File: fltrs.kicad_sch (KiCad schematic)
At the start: 51 parts, among them U3 CPC1117N, U4 MCP6002, U5 MCP4451-503-ST, U6 MCP6002, U7 MCP6002

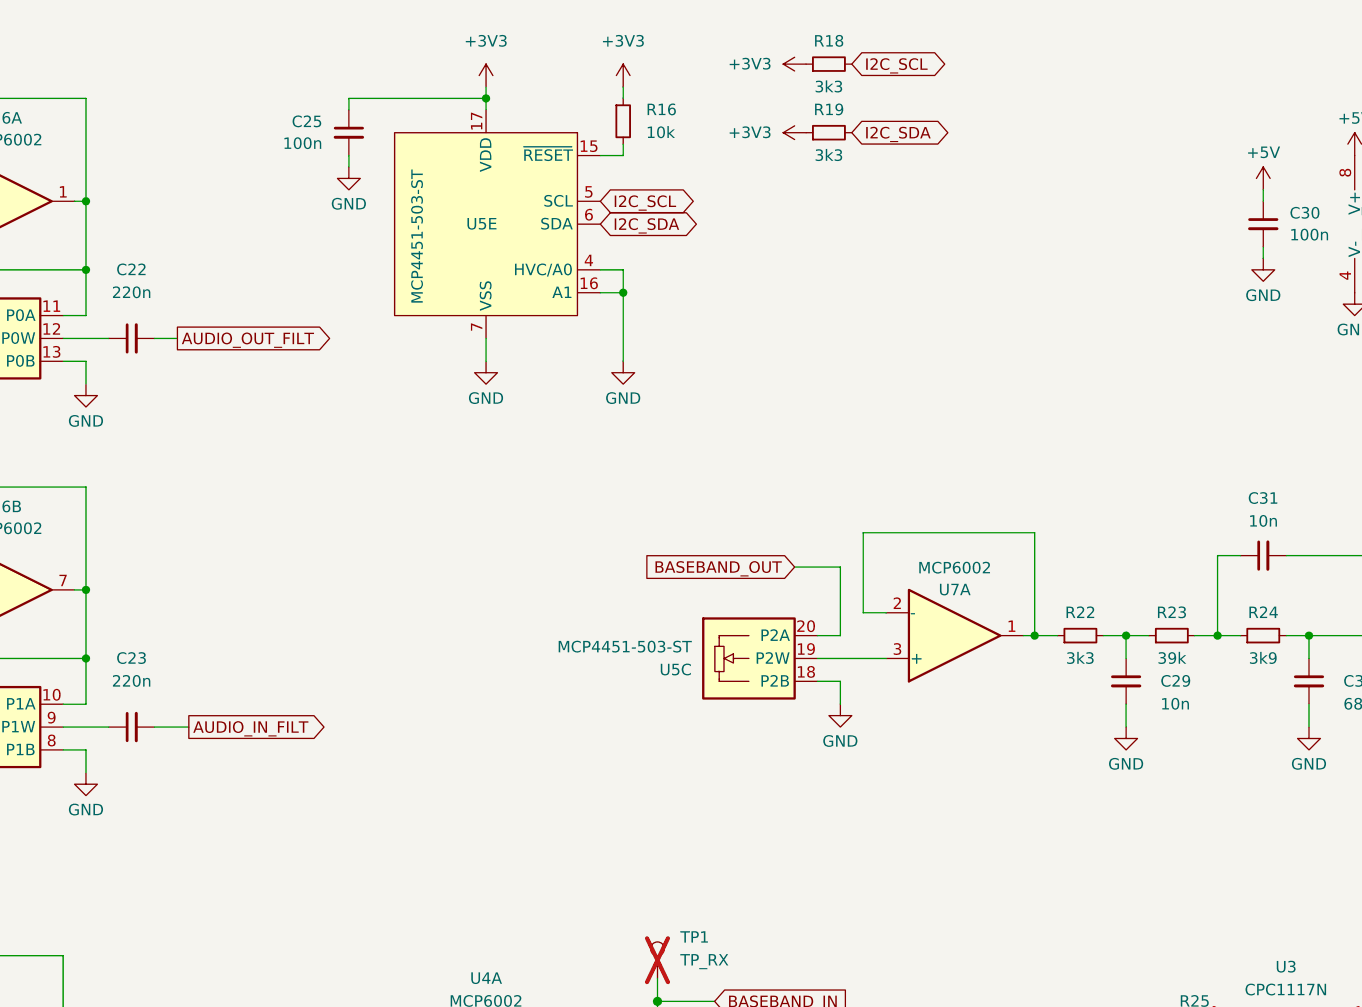
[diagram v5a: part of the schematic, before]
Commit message: PA2 Bias add, USB conn add.
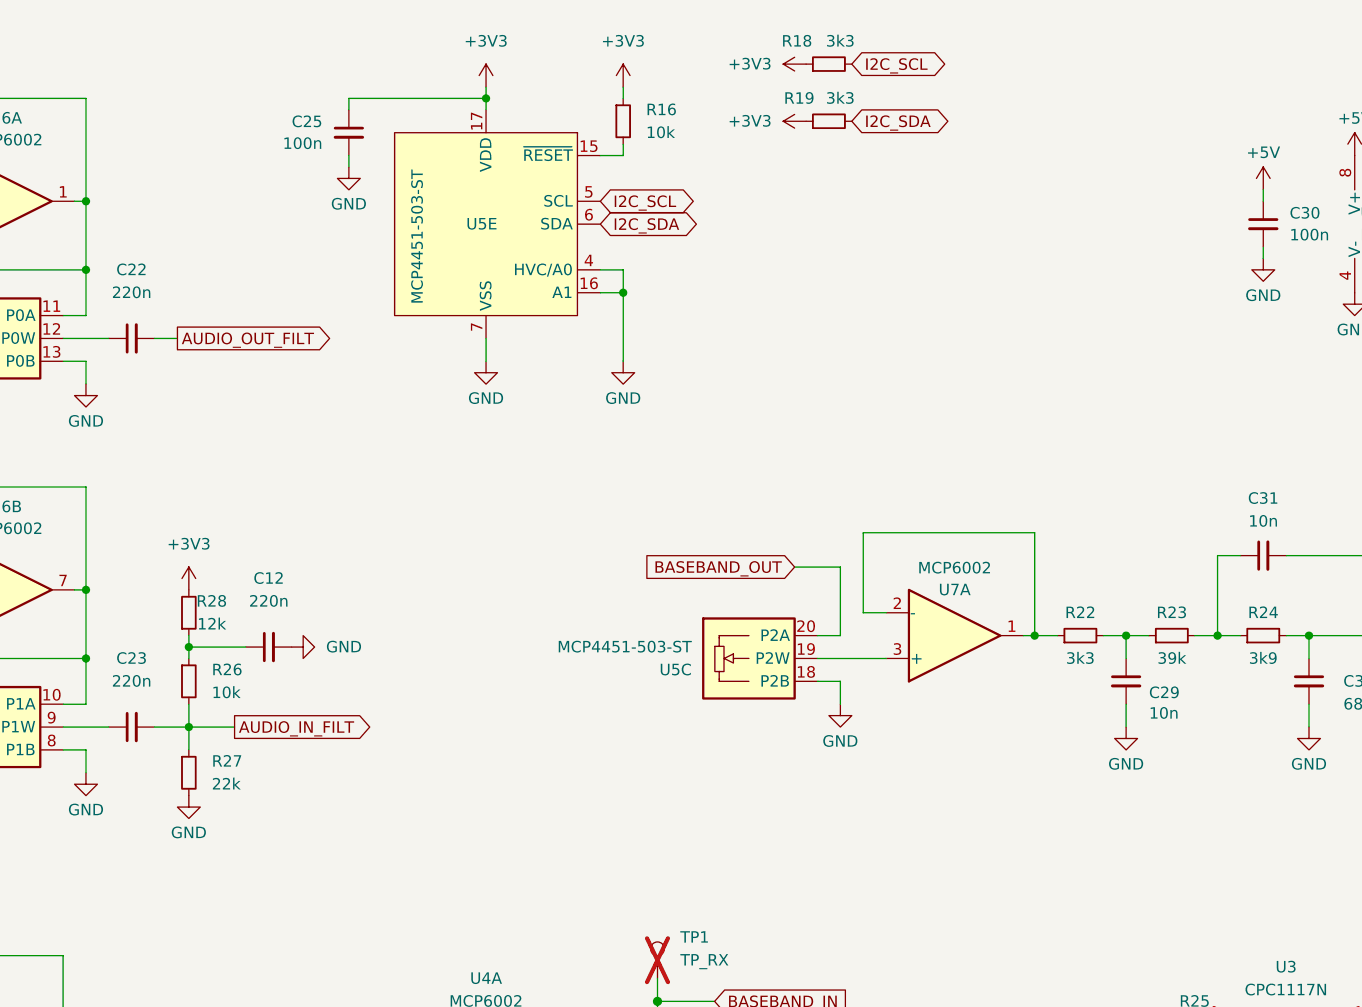
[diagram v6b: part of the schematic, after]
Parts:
- added C12: 220n, Capacitor_SMD:C_0402_1005Metric, symbol Device:C_Small
- added R26: 10k, Resistor_SMD:R_0402_1005Metric, symbol Device:R_Small
- added R27: 22k, Resistor_SMD:R_0402_1005Metric, symbol Device:R_Small
- added R28: 12k, Resistor_SMD:R_0402_1005Metric, symbol Device:R_Small
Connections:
- net +3V3: now also R28.2
- net AUDIO_IN_FILT: now also R26.2, R27.1
- net GND: now also C12.2, R27.2
- new net: C12.1, R26.1, R28.1
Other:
- title: Micro17 - OpenRTX on a Module -> Micro17 - OpenRTX on a Module for Icom Radios
- moved on the sheet: R19

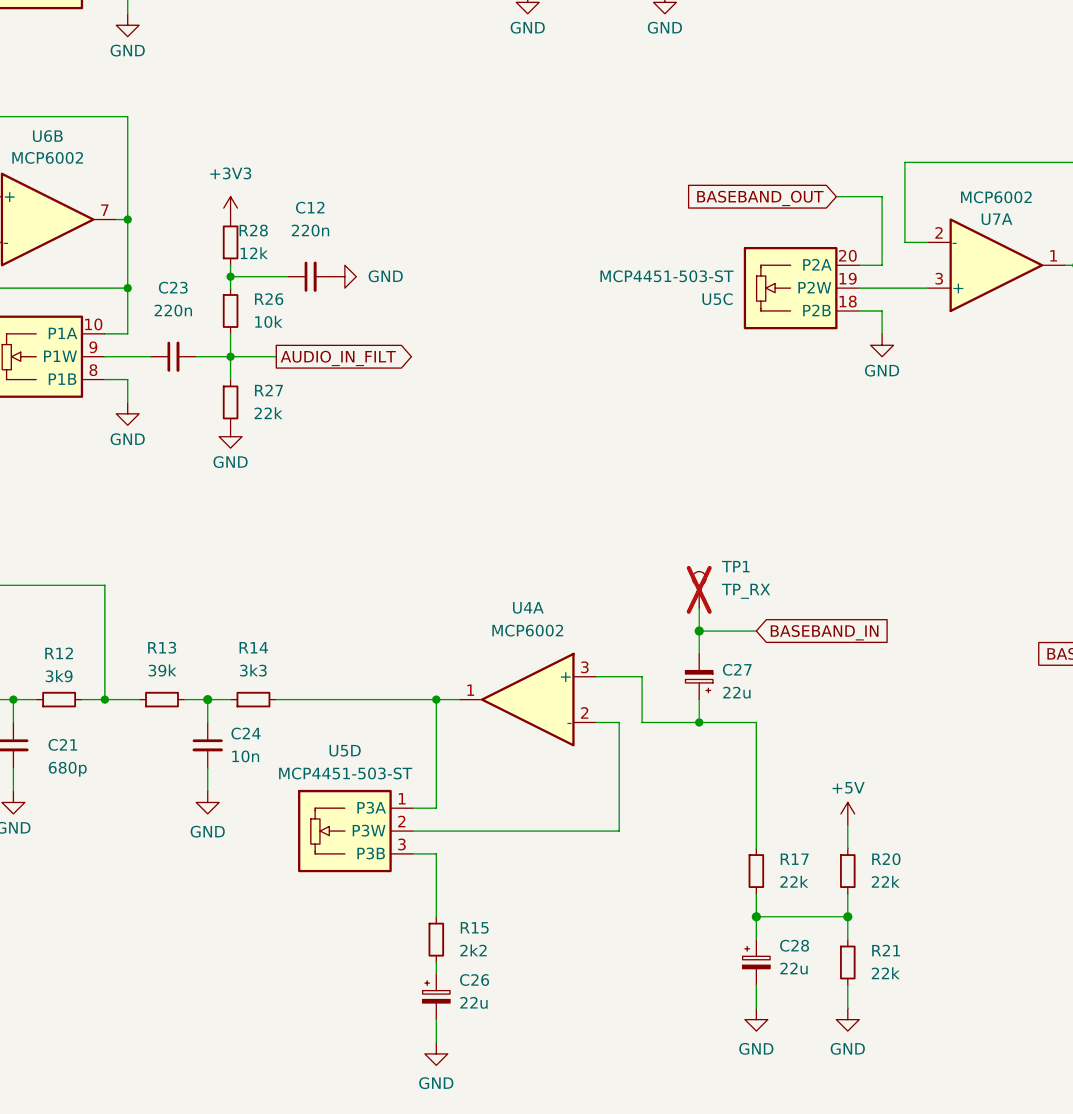
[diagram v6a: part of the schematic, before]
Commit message: Changed PA2 bias circuit
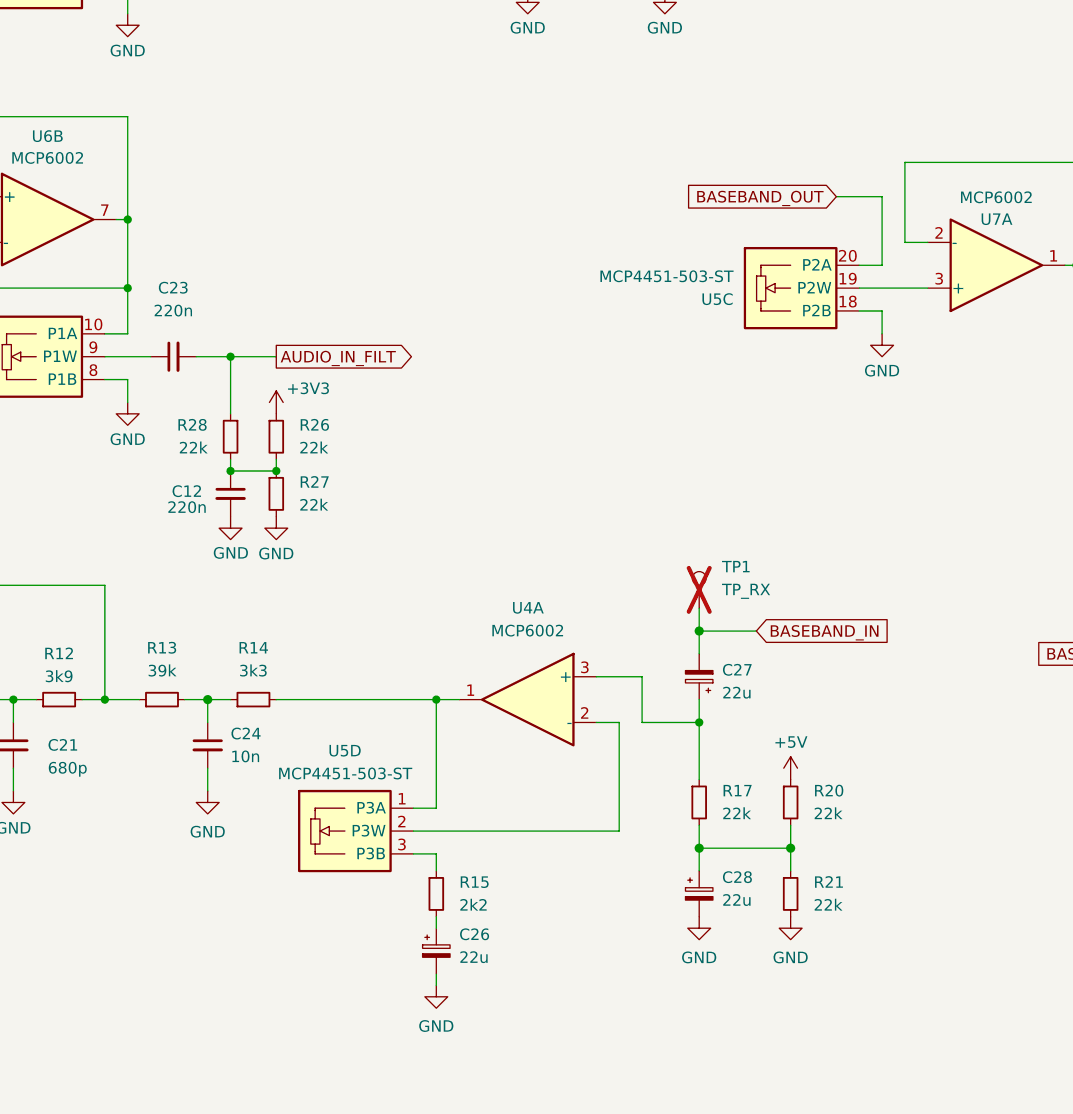
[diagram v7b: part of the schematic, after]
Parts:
- R26: value 10k -> 22k; LCSC C102749 -> C2909337; MPN (none) -> Generic R/22k/0603
- R28: value 12k -> 22k; LCSC C25752 -> C2909337; MPN (none) -> Generic R/22k/0603
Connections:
- net +3V3: now also R26.1; no longer R28.2
- net AUDIO_IN_FILT: now also R28.1; no longer R26.2, R27.1
- new net: C12.1, R26.2, R27.1, R28.2
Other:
- moved on the sheet: C12, C26, C28, R15, R17, R20, R21, R27

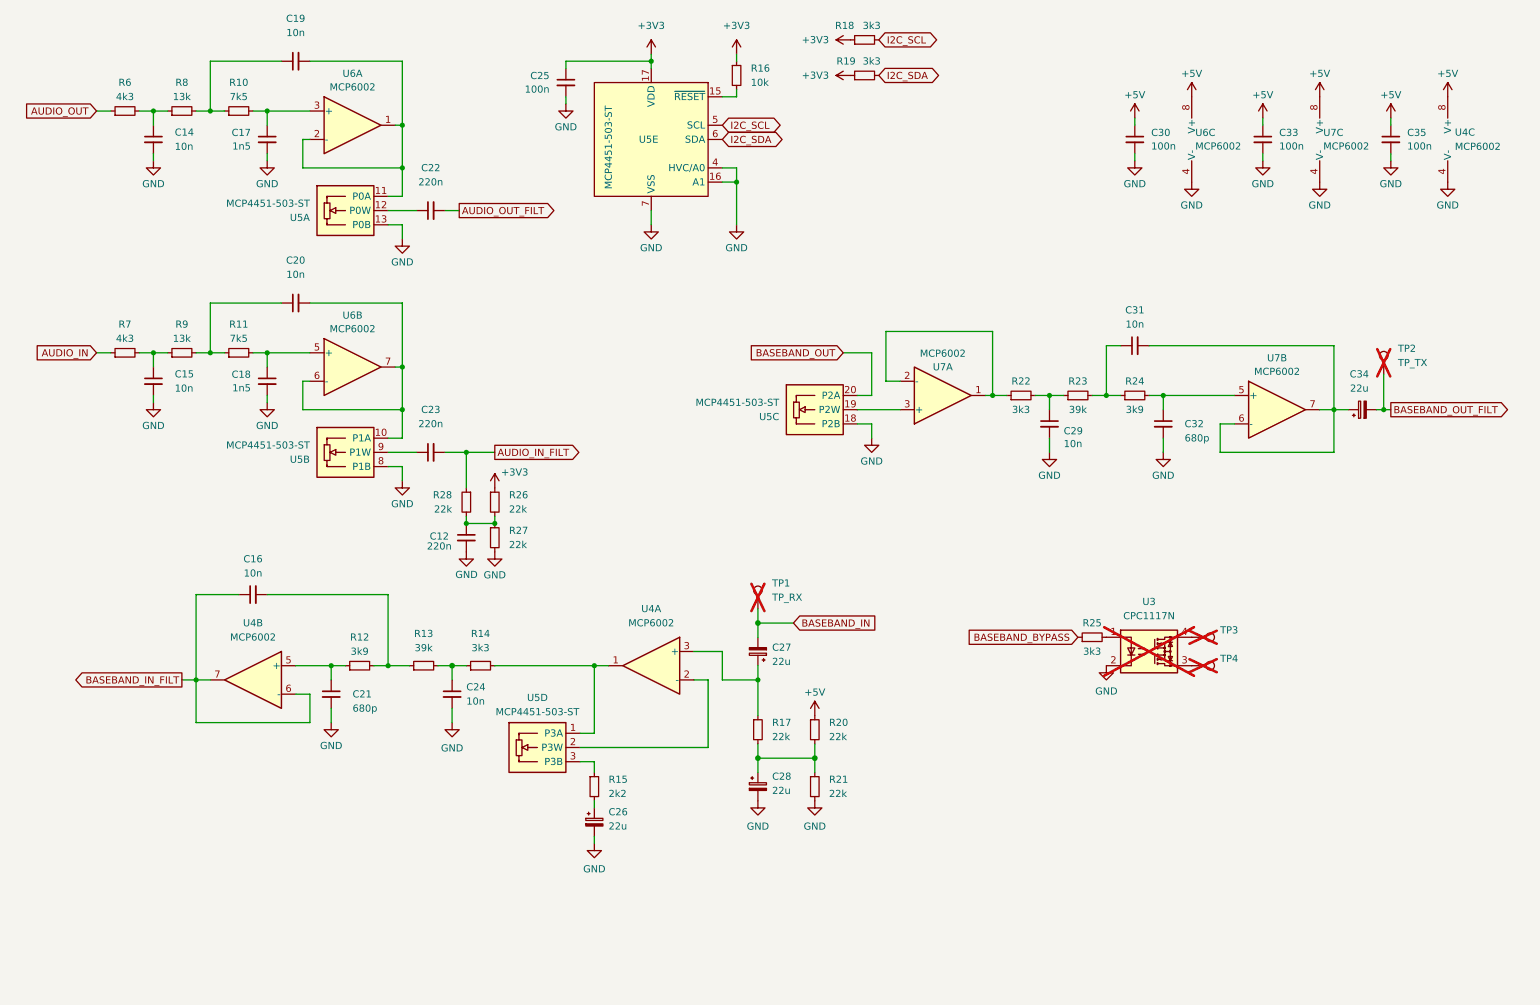
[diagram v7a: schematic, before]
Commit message: cosmetic changes to the schematic layout
- R25 - DNP
- PDF render update
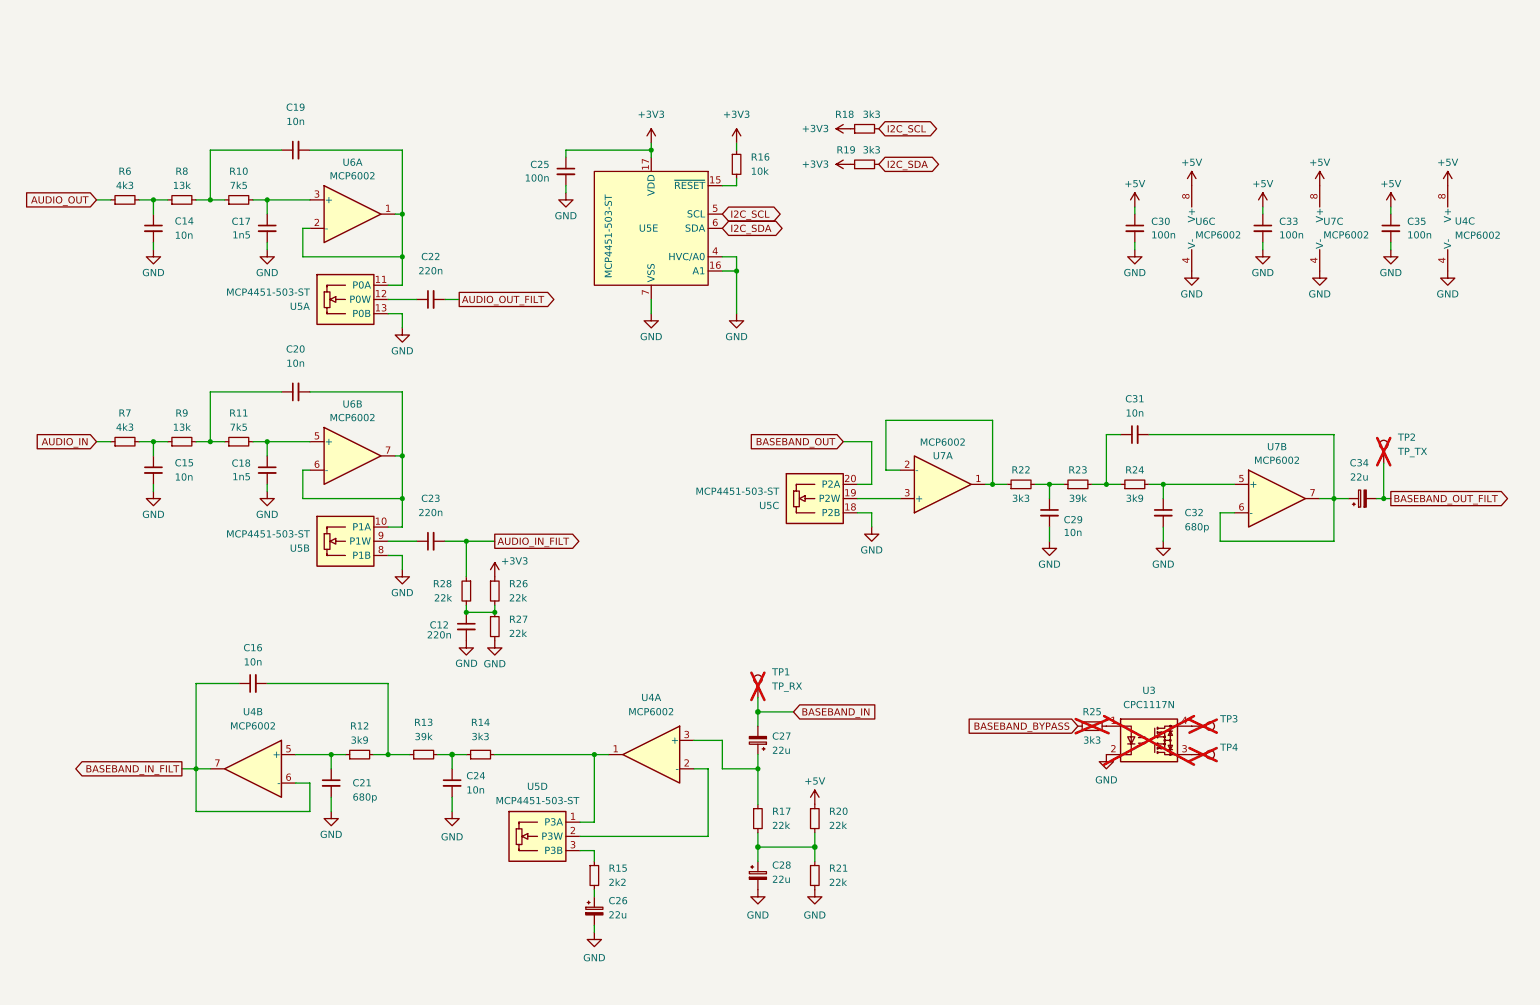
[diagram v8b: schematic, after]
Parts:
- R25: now not fitted
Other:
- company: Wojciech Kaczmarski SP5WWP et al. -> Wojciech SP5WWP, Mano ON6RF, Mutlu TA1MD et al.
- title: Micro17 - OpenRTX on a Module for Icom Radios -> Micro17 - OpenRTX on a Module for ICOM radios
- moved on the sheet: C12, C14, C15, C16, C17, C18, C19, C20, C21, C22, C23, C24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
